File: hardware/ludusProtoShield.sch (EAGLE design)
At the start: 54 parts, among them U1 ARDUINO, U3 TB6612FNG

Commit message: Updated design to resolve all issues
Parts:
- removed FRAME1: FRAME-LETTER, SparkFun-Aesthetics:FRAME-LETTER
- removed SJ1, SJ2: JUMPER-PAD-3-2OF3_NC_BY_PASTE, SparkFun-Passives:JUMPER-PAD-3-2OF3_NC_BY_PASTE
- added FRAME2: FRAME-LEDGER, SparkFun-Aesthetics:FRAME-LEDGER
- added S1, S2: (no value), SparkFun-Electromechanical:SWITCH-SPDTSMD
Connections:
- net N$20 renamed BIN2
- net ANALOG_PWR_RAIL: now also S1.P; no longer SJ2.2
- net FUSED_VCC: now also S1.S, S2.S; no longer SJ1.3, SJ2.3
- net FUSED_VIN: now also S1.O, S2.O; no longer SJ1.1, SJ2.1
- net PWR_RAIL: now also S2.P; no longer SJ1.2
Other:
- note added: "Analog 3 Pin Headers"
- note added: "Digital I/O 3 Pin Headers"
- note added: "Jumpers to select between SCL / A5 and SDA / A4 pins on the new R3 footprint -- for Leonardo compatibility."
- note added: "Power Select for VIN vs. 5V"
- note added: "v02"
- note removed: "v11"
- moved on the sheet: C1, C2, C4, F1, F2, JP0, JP1, JP11, JP12, JP13, JP14, JP15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

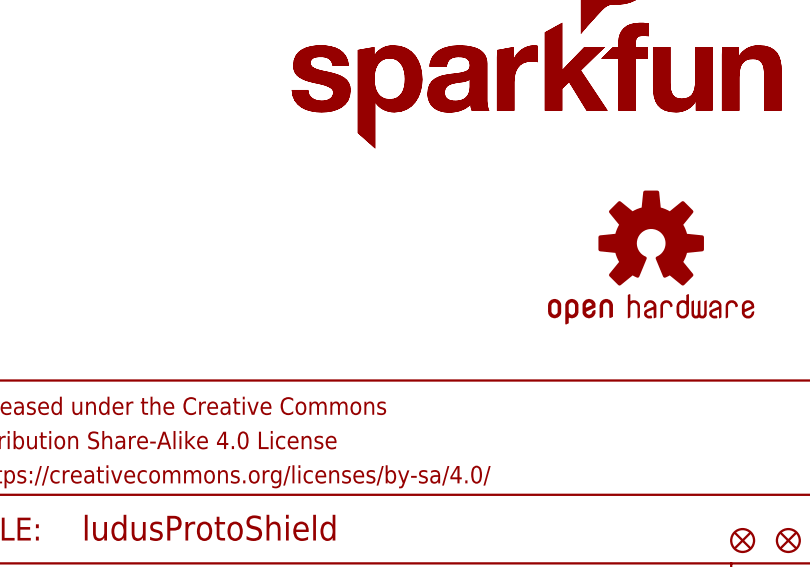
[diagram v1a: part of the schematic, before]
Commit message: Fixed ERC & Board Consistency errors
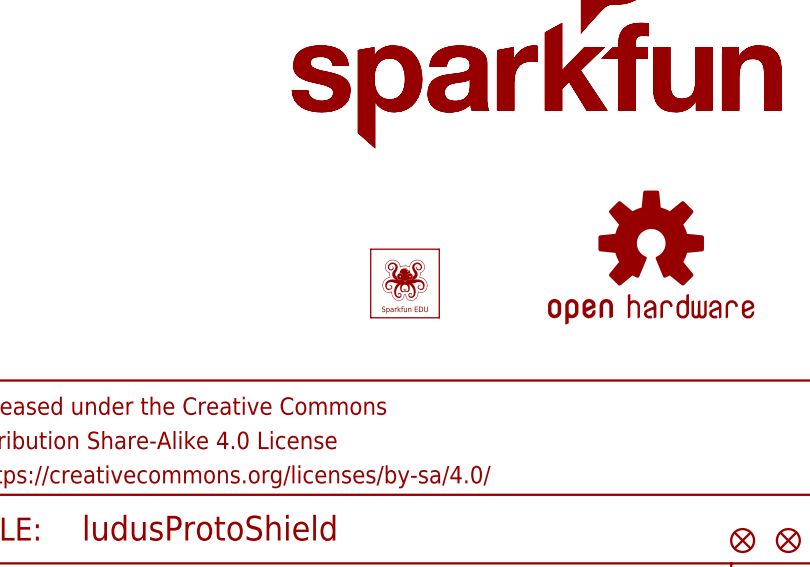
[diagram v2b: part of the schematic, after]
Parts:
- U$1: value SFE_LUDUS -> SFE_LUDUSSFE_LUDUS-M; device SparkFun-Aesthetics:SFE_LUDUS -> SparkFun-Aesthetics:SFE_LUDUSSFE_LUDUS-M
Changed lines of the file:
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@@
 <grid distance="0.1" unitdist="inch" unit="inch" style="lines" multiple="1" display="no" altdistance="0.01" altunitdist="inch" altunit="inch"/>
 <layers>
-<layer number="1" name="Top" color="4" fill="1" visible="no" active="no"/>
-<layer number="2" name="Route2" color="1" fill="3" visible="no" active="no"/>
-<layer number="3" name="Route3" color="4" fill="3" visible="no" active="no"/>
-<layer number="4" name="Route4" color="1" fill="4" visible="no" active="no"/>
-<layer number="5" name="Route5" color="4" fill="4" visible="no" active="no"/>
-<layer number="6" name="Route6" color="1" fill="8" visible="no" active="no"/>
-<layer number="7" name="Route7" color="4" fill="8" visible="no" active="no"/>
-<layer number="8" name="Route8" color="1" fill="2" visible="no" active="no"/>
-<layer number="9" name="Route9" color="4" fill="2" visible="no" active="no"/>
-<layer number="10" name="Route10" color="1" fill="7" visible="no" active="no"/>
-<layer number="11" name="Route11" color="4" fill="7" visible="no" active="no"/>
-<layer number="12" name="Route12" color="1" fill="5" visible="no" active="no"/>
-<layer number="13" name="Route13" color="4" fill="5" visible="no" active="no"/>
-<layer number="14" name="Route14" color="1" fill="6" visible="no" active="no"/>
-<layer number="15" name="Route15" color="4" fill="6" visible="no" active="no"/>
-<layer number="16" name="Bottom" color="1" fill="1" visible="no" active="no"/>
-<layer number="17" name="Pads" color="2" fill="1" visible="no" active="no"/>
-<layer number="18" name="Vias" color="2" fill="1" visible="no" active="no"/>
-<layer number="19" name="Unrouted" color="6" fill="1" visible="no" active="no"/>
-<layer number="20" name="Dimension" color="15" fill="1" visible="no" active="no"/>
-<layer number="21" name="tPlace" color="16" fill="1" visible="no" active="no"/>
-<layer number="22" name="bPlace" color="14" fill="1" visible="no" active="no"/>
-<layer number="23" name="tOrigins" color="15" fill="1" visible="no" active="no"/>
-<layer number="24" name="bOrigins" color="15" fill="1" visible="no" active="no"/>
-<layer number="25" name="tNames" color="7" fill="1" visible="no" active="no"/>
-<layer number="26" name="bNames" color="7" fill="1" visible="no" active="no"/>
-<layer number="27" name="tValues" color="7" fill="1" visible="no" active="no"/>
-<layer number="28" name="bValues" color="7" fill="1" visible="no" active="no"/>
+<layer number="1" name="Top" color="4" fill="1" visible="yes" active="no"/>
+<layer number="2" name="Route2" color="1" fill="3" visible="yes" active="no"/>
+<layer number="3" name="Route3" color="4" fill="3" visible="yes" active="no"/>
+<layer number="4" name="Route4" color="1" fill="4" visible="yes" active="no"/>
+<layer number="5" name="Route5" color="4" fill="4" visible="yes" active="no"/>
+<layer number="6" name="Route6" color="1" fill="8" visible="yes" active="no"/>
+<layer number="7" name="Route7" color="4" fill="8" visible="yes" active="no"/>
+<layer number="8" name="Route8" color="1" fill="2" visible="yes" active="no"/>
+<layer number="9" name="Route9" color="4" fill="2" visible="yes" active="no"/>
+<layer number="10" name="Route10" color="1" fill="7" visible="yes" active="no"/>
+<layer number="11" name="Route11" color="4" fill="7" visible="yes" active="no"/>
+<layer number="12" name="Route12" color="1" fill="5" visible="yes" active="no"/>
+<layer number="13" name="Route13" color="4" fill="5" visible="yes" active="no"/>
+<layer number="14" name="Route14" color="1" fill="6" visible="yes" active="no"/>
+<layer number="15" name="Route15" color="4" fill="6" visible="yes" active="no"/>
+<layer number="16" name="Bottom" color="1" fill="1" visible="yes" active="no"/>
+<layer number="17" name="Pads" color="2" fill="1" visible="yes" active="no"/>
+<layer number="18" name="Vias" color="2" fill="1" visible="yes" active="no"/>
+<layer number="19" name="Unrouted" color="6" fill="1" visible="yes" active="no"/>
+<layer number="20" name="Dimension" color="15" fill="1" visible="yes" active="no"/>
+<layer number="21" name="tPlace" color="16" fill="1" visible="yes" active="no"/>
+<layer number="22" name="bPlace" color="14" fill="1" visible="yes" active="no"/>
+<layer number="23" name="tOrigins" color="15" fill="1" visible="yes" active="no"/>
+<layer number="24" name="bOrigins" color="15" fill="1" visible="yes" active="no"/>
+<layer number="25" name="tNames" color="7" fill="1" visible="yes" active="no"/>
+<layer number="26" name="bNames" color="7" fill="1" visible="yes" active="no"/>
+<layer number="27" name="tValues" color="7" fill="1" visible="yes" active="no"/>
+<layer number="28" name="bValues" color="7" fill="1" visible="yes" active="no"/>
 <layer number="29" name="tStop" color="7" fill="3" visible="no" active="no"/>
 <layer number="30" name="bStop" color="7" fill="6" visible="no" active="no"/>
@@
 <layer number="35" name="tGlue" color="7" fill="4" visible="no" active="no"/>
 <layer number="36" name="bGlue" color="7" fill="5" visible="no" active="no"/>
-<layer number="37" name="tTest" color="7" fill="1" visible="no" active="no"/>
-<layer number="38" name="bTest" color="7" fill="1" visible="no" active="no"/>
+<layer number="37" name="tTest" color="7" fill="1" visible="yes" active="no"/>
+<layer number="38" name="bTest" color="7" fill="1" visible="yes" active="no"/>
 <layer number="39" name="tKeepout" color="4" fill="11" visible="no" active="no"/>
 <layer number="40" name="bKeepout" color="1" fill="11" visible="no" active="no"/>
@@
 <layer number="44" name="Drills" color="7" fill="1" visible="no" active="no"/>
 <layer number="45" name="Holes" color="7" fill="1" visible="no" active="no"/>
-<layer number="46" name="Milling" color="3" fill="1" visible="no" active="no"/>
-<layer number="47" name="Measures" color="7" fill="1" visible="no" active="no"/>
-<layer number="48" name="Document" color="7" fill="1" visible="no" active="no"/>
-<layer number="49" name="Reference" color="7" fill="1" visible="no" active="no"/>
-<layer number="50" name="dxf" color="7" fill="1" visible="no" active="no"/>
-<layer number="51" name="tDocu" color="6" fill="1" visible="no" active="no"/>
-<layer number="52" name="bDocu" color="7" fill="1" visible="no" active="no"/>
-<layer number="53" name="tGND_GNDA" color="7" fill="9" visible="no" active="no"/>
-<layer number="54" name="bGND_GNDA" color="1" fill="9" visible="no" active="no"/>
-<layer number="56" name="wert" color="7" fill="1" visible="no" active="no"/>
-<layer number="57" name="tCAD" color="7" fill="1" visible="no" active="no"/>
+<layer number="46" name="Milling" color="3" fill="1" visible="yes" active="no"/>
+<layer number="47" name="Measures" color="7" fill="1" visible="yes" active="no"/>
+<layer number="48" name="Document" color="7" fill="1" visible="yes" active="no"/>
+<layer number="49" name="Reference" color="7" fill="1" visible="yes" active="no"/>
+<layer number="50" name="dxf" color="7" fill="1" visible="yes" active="no"/>
+<layer number="51" name="tDocu" color="6" fill="1" visible="yes" active="no"/>
+<layer number="52" name="bDocu" color="7" fill="1" visible="yes" active="no"/>
+<layer number="53" name="tGND_GNDA" color="7" fill="9" visible="yes" active="no"/>
+<layer number="54" name="bGND_GNDA" color="1" fill="9" visible="yes" active="no"/>
+<layer number="56" name="wert" color="7" fill="1" visible="yes" active="no"/>
+<layer number="57" name="tCAD" color="7" fill="1" visible="yes" active="no"/>
 <layer number="90" name="Modules" color="5" fill="1" visible="yes" active="yes"/>
 <layer number="91" name="Nets" color="2" fill="1" visible="yes" active="yes"/>
@@
 <layer number="223" name="223bmp" color="24" fill="1" visible="no" active="no"/>
 <layer number="224" name="224bmp" color="25" fill="1" visible="no" active="no"/>
+<layer number="225" name="225bmp" color="7" fill="1" visible="yes" active="yes"/>
+<layer number="226" name="226bmp" color="7" fill="1" visible="yes" active="yes"/>
+<layer number="227" name="227bmp" color="7" fill="1" visible="yes" active="yes"/>
+<layer number="228" name="228bmp" color="7" fill="1" visible="yes" active="yes"/>
+<layer number="229" name="229bmp" color="7" fill="1" visible="yes" active="yes"/>
+<layer number="230" name="230bmp" color="7" fill="1" visible="yes" active="yes"/>
+<layer number="231" name="231bmp" color="7" fill="1" visible="yes" active="yes"/>
 <layer number="248" name="Housing" color="7" fill="1" visible="yes" active="yes"/>
 <layer number="249" name="Edge" color="7" fill="1" visible="yes" active="yes"/>
@@
 <part name="SJ3" library="SparkFun-Passives" deviceset="JUMPER-PAD-3-NC_BY_TRACE" device=""/>
 <part name="SJ4" library="SparkFun-Passives" deviceset="JUMPER-PAD-3-NC_BY_TRACE" device=""/>
-<part name="U$1" library="SparkFun-Aesthetics" deviceset="SFE_LUDUS" device=""/>
+<part name="U$1" library="SparkFun-Aesthetics" deviceset="SFE_LUDUS" device="SFE_LUDUS-M"/>
 <part name="LOGO3" library="SparkFun-Aesthetics" deviceset="SFE_LOGO_FLAME" device=".2COP"/>
 <part name="LOGO4" library="SparkFun-Aesthetics" deviceset="SFE_LOGO_NAME_FLAME" device=".1_INCH" value="SFE_LOGO_NAME_FLAME.1_INCH"/>
@@
 <instance part="SJ3" gate="G$1" x="154.94" y="88.9" rot="R180"/>
 <instance part="SJ4" gate="G$1" x="154.94" y="116.84" rot="R180"/>
-<instance part="U$1" gate="G$1" x="412.131559375" y="93.295265625" rot="R90"/>
+<instance part="U$1" gate="G$1" x="352.375265625" y="24.748440625"/>
 <instance part="LOGO3" gate="G$1" x="375.412" y="55.88"/>
 <instance part="LOGO4" gate="G$1" x="342.9" y="43.18"/>

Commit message: Minor silk changes
Updated pin silks to 0.04 for all ones that don't interfere with other
masks.

Added to bSilk labels for the motor out
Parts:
- JP20: device SparkFun-Connectors:M04LOCK -> SparkFun-Connectors:M04PTH
- JP22: device SparkFun-Connectors:M04PTH -> SparkFun-Connectors:M04LOCK
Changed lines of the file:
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@@
 <?xml version="1.0" encoding="utf-8"?>
 <!DOCTYPE eagle SYSTEM "eagle.dtd">
-<eagle version="6.5.0">
+<eagle version="7.2.0">
 <drawing>
 <settings>
@@
 <part name="FID1" library="SparkFun-Aesthetics" deviceset="FIDUCIAL" device="1X2" value="FIDUCIAL1X2"/>
 <part name="FID2" library="SparkFun-Aesthetics" deviceset="FIDUCIAL" device="1X2" value="FIDUCIAL1X2"/>
-<part name="JP20" library="SparkFun-Connectors" deviceset="M04" device="LOCK"/>
+<part name="JP20" library="SparkFun-Connectors" deviceset="M04" device="PTH"/>
 <part name="LOGO1" library="SparkFun-Aesthetics" deviceset="OSHW-LOGO" device="M"/>
 <part name="LOGO2" library="SparkFun-Aesthetics" deviceset="SFE_LOGO_NAME_FLAME" device=".1_INCH" value="SFE_LOGO_NAME_FLAME.1_INCH"/>
-<part name="JP22" library="SparkFun-Connectors" deviceset="M04" device="PTH"/>
+<part name="JP22" library="SparkFun-Connectors" deviceset="M04" device="LOCK"/>
 <part name="SJ3" library="SparkFun-Passives" deviceset="JUMPER-PAD-3-NC_BY_TRACE" device=""/>
 <part name="SJ4" library="SparkFun-Passives" deviceset="JUMPER-PAD-3-NC_BY_TRACE" device=""/>

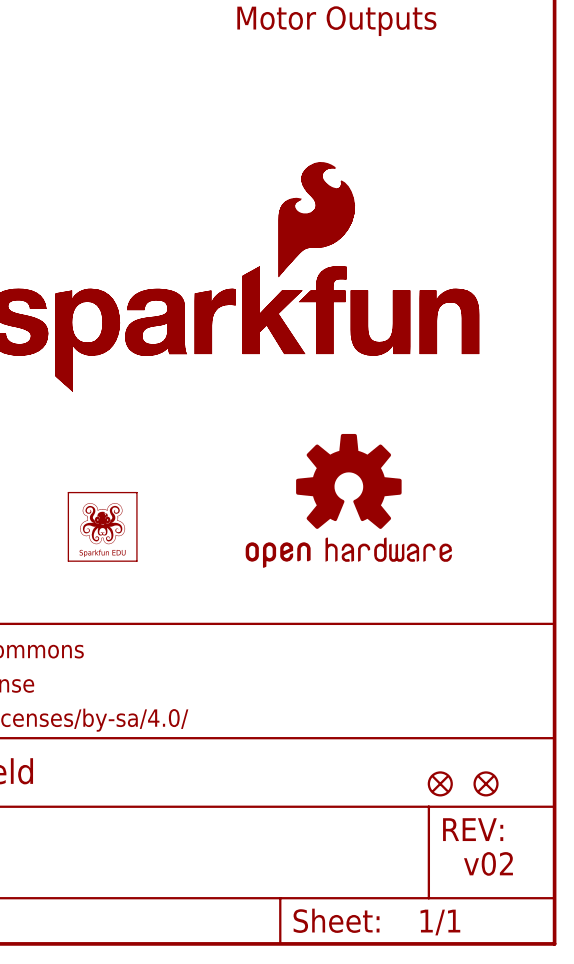
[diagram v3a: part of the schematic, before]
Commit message: Final changes to v1.0
Final design changes from engineering design review. Ready for reds.
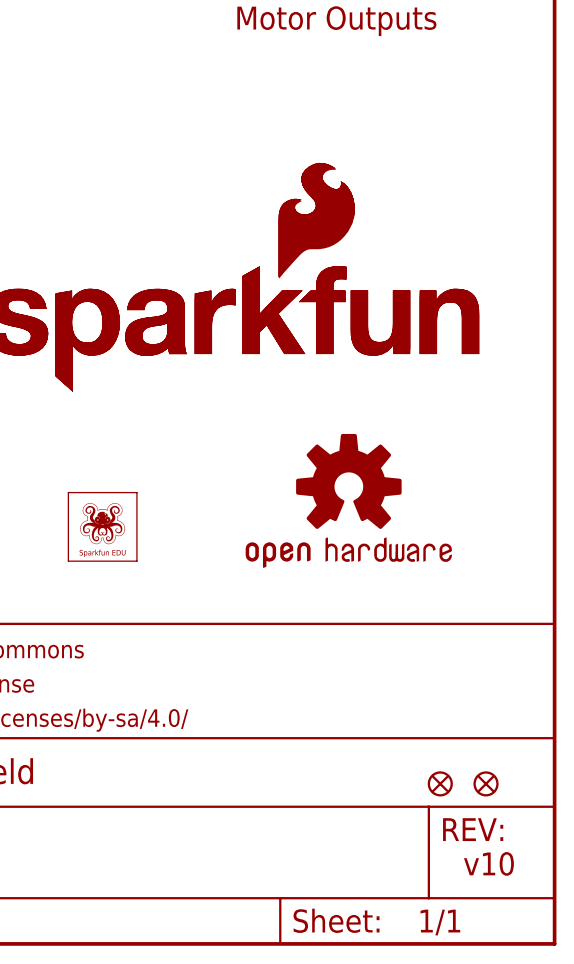
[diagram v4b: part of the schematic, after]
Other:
- note added: "v10"
- note removed: "v02"
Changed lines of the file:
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@@
 <part name="SJ4" library="SparkFun-Passives" deviceset="JUMPER-PAD-3-NC_BY_TRACE" device=""/>
 <part name="U$1" library="SparkFun-Aesthetics" deviceset="SFE_LUDUS" device="SFE_LUDUS-M"/>
-<part name="LOGO3" library="SparkFun-Aesthetics" deviceset="SFE_LOGO_FLAME" device=".2COP"/>
 <part name="LOGO4" library="SparkFun-Aesthetics" deviceset="SFE_LOGO_NAME_FLAME" device=".1_INCH" value="SFE_LOGO_NAME_FLAME.1_INCH"/>
 <part name="JP23" library="SparkFun-Connectors" deviceset="M04" device="LOCK"/>
@@
 <part name="S1" library="SparkFun-Electromechanical" deviceset="SWITCH-SPDT" device="SMD"/>
 <part name="S2" library="SparkFun-Electromechanical" deviceset="SWITCH-SPDT" device="SMD"/>
+<part name="LOGO3" library="SparkFun-Aesthetics" deviceset="SFE_LOGO_FLAME" device=".2COP" value="SFE_LOGO_FLAME.2COP"/>
 </parts>
 <sheets>
@@
 <text x="370.84" y="83.82" size="2.54" layer="94">Motor Outputs</text>
 <text x="325.12" y="-10.16" size="2.54" layer="94">B. Huang</text>
-<text x="396.24" y="-10.16" size="2.54" layer="94">v02</text>
+<text x="396.24" y="-10.16" size="2.54" layer="94">v10</text>
 <wire x1="-25.4" y1="177.8" x2="78.74" y2="177.8" width="0.2032" layer="97" style="longdash"/>
 <wire x1="78.74" y1="177.8" x2="134.62" y2="177.8" width="0.2032" layer="97" style="longdash"/>
@@
 <instance part="SJ4" gate="G$1" x="154.94" y="116.84" rot="R180"/>
 <instance part="U$1" gate="G$1" x="352.375265625" y="24.748440625"/>
-<instance part="LOGO3" gate="G$1" x="375.412" y="55.88"/>
 <instance part="LOGO4" gate="G$1" x="342.9" y="43.18"/>
 <instance part="JP23" gate="G$1" x="259.08" y="111.76"/>
@@
 <instance part="S1" gate="1" x="109.22" y="152.4"/>
 <instance part="S2" gate="1" x="33.02" y="152.4"/>
+<instance part="LOGO3" gate="G$1" x="375.412" y="55.626"/>
 </instances>
 <busses>
